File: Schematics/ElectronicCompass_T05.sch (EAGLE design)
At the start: 60 parts, among them Q1 SPB80P06P, Q2 SPB80P06P, Q3 SPB80P06P, Q4 SPB80P06P, U1 ATMEGA32U4, X1 USBSMD

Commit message: board layout continued
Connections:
- net GND: no longer U$1.GND, U$1.NTC
- net N$16: now also U$1.BAT; no longer U$1.GATE
- net N$4: no longer U$1.CLPROG
- net N$5: now also U$1.GATE; no longer U$1.BAT
- net VCC: no longer U$1.ILIM0, U$1.ILIM1
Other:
- moved on the sheet: R4
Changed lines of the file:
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@@
 <part name="GND14" library="supply1" deviceset="GND" device=""/>
 <part name="C2" library="rcl" deviceset="C-US" device="C0805" value="10nF"/>
-<part name="U$1" library="LTC4067" deviceset="LTC4067" device=""/>
 <part name="C3" library="rcl" deviceset="C-US" device="C0805" value="0.1uF"/>
 <part name="TP26" library="testpad" deviceset="TP" device="TP06R"/>
 <part name="TP27" library="testpad" deviceset="TP" device="TP06R"/>
 <part name="TP28" library="testpad" deviceset="TP" device="TP06R"/>
+<part name="U$1" library="LTC4067" deviceset="LTC4067" device=""/>
 </parts>
 <sheets>
@@
 <frame x1="-25.4" y1="-121.92" x2="276.86" y2="88.9" columns="8" rows="5" layer="97"/>
 <text x="243.84" y="-40.64" size="1.778" layer="97">LCD Mounting/TP</text>
-<text x="53.34" y="27.94" size="1.778" layer="97">LTC4067</text>
+<text x="50.8" y="27.94" size="1.778" layer="97">LTC4067</text>
 <text x="210.82" y="10.16" size="1.778" layer="97">LSM303DLM</text>
 <text x="213.36" y="-66.04" size="1.778" layer="97">Nokia 5110</text>
@@
 <instance part="JP6" gate="G$1" x="175.26" y="-86.36"/>
 <instance part="JP7" gate="G$1" x="182.88" y="-86.36"/>
-<instance part="R4" gate="G$1" x="30.48" y="17.78" rot="R90"/>
+<instance part="R4" gate="G$1" x="30.48" y="15.24" rot="R90"/>
 <instance part="R5" gate="G$1" x="27.94" y="55.88"/>
 <instance part="R6" gate="G$1" x="71.12" y="17.78" rot="R270"/>
@@
 <instance part="GND9" gate="1" x="50.8" y="10.16"/>
 <instance part="GND15" gate="1" x="71.12" y="10.16"/>
-<instance part="GND16" gate="1" x="30.48" y="10.16"/>
-<instance part="P+5" gate="VCC" x="25.4" y="38.1"/>
+<instance part="GND16" gate="1" x="30.48" y="7.62"/>
+<instance part="P+5" gate="VCC" x="25.4" y="35.56"/>
 <instance part="LED1" gate="G$1" x="20.32" y="50.8" rot="R180"/>
 <instance part="Q1" gate="G$1" x="12.7" y="48.26" rot="MR270"/>
@@
 <instance part="C12" gate="G$1" x="76.2" y="-17.78"/>
 <instance part="GND17" gate="1" x="76.2" y="-25.4"/>
-<instance part="GND18" gate="1" x="33.02" y="35.56"/>
+<instance part="GND18" gate="1" x="33.02" y="33.02"/>
 <instance part="G1" gate="G$1" x="81.28" y="30.48" rot="R90"/>
 <instance part="GND19" gate="1" x="81.28" y="22.86"/>
@@
 <instance part="GND14" gate="1" x="5.08" y="35.56"/>
 <instance part="C2" gate="G$1" x="10.16" y="68.58"/>
-<instance part="U$1" gate="G$1" x="50.8" y="40.64" rot="R270"/>
 <instance part="C3" gate="G$1" x="121.92" y="7.62"/>
 <instance part="TP26" gate="G$1" x="180.34" y="-33.02" rot="R270"/>
 <instance part="TP27" gate="G$1" x="180.34" y="-48.26" rot="R270"/>
 <instance part="TP28" gate="G$1" x="180.34" y="-43.18" rot="R270"/>
+<instance part="U$1" gate="G$1" x="50.8" y="45.72" rot="R270"/>
 </instances>
 <busses>
@@
 <pinref part="GND18" gate="1" pin="GND"/>
 <pinref part="C5" gate="G$1" pin="2"/>
-<wire x1="30.48" y1="38.1" x2="33.02" y2="38.1" width="0.1524" layer="91"/>
-<pinref part="U$1" gate="G$1" pin="NTC"/>
-<junction x="33.02" y="38.1"/>
+<wire x1="30.48" y1="38.1" x2="30.48" y2="35.56" width="0.1524" layer="91"/>
+<wire x1="30.48" y1="35.56" x2="33.02" y2="35.56" width="0.1524" layer="91"/>
 </segment>
 <segment>
 <pinref part="C11" gate="G$1" pin="2"/>
 <pinref part="GND14" gate="1" pin="GND"/>
-</segment>
-<segment>
-<pinref part="GND9" gate="1" pin="GND"/>
-<pinref part="U$1" gate="G$1" pin="GND"/>
 </segment>
 <segment>
@@
 </segment>
 <segment>
-<wire x1="33.02" y1="27.94" x2="25.4" y2="27.94" width="0.1524" layer="91"/>
+<wire x1="33.02" y1="25.4" x2="25.4" y2="25.4" width="0.1524" layer="91"/>
 <pinref part="P+5" gate="VCC" pin="VCC"/>
-<wire x1="25.4" y1="27.94" x2="25.4" y2="33.02" width="0.1524" layer="91"/>
-<wire x1="25.4" y1="33.02" x2="25.4" y2="35.56" width="0.1524" layer="91"/>
-<wire x1="33.02" y1="33.02" x2="25.4" y2="33.02" width="0.1524" layer="91"/>
-<junction x="25.4" y="33.02"/>
-<pinref part="U$1" gate="G$1" pin="ILIM0"/>
-<pinref part="U$1" gate="G$1" pin="ILIM1"/>
+<wire x1="25.4" y1="25.4" x2="25.4" y2="30.48" width="0.1524" layer="91"/>
+<wire x1="25.4" y1="30.48" x2="25.4" y2="33.02" width="0.1524" layer="91"/>
+<wire x1="33.02" y1="30.48" x2="25.4" y2="30.48" width="0.1524" layer="91"/>
+<junction x="25.4" y="30.48"/>
 </segment>
 </net>
@@
 <segment>
 <pinref part="R4" gate="G$1" pin="2"/>
-<wire x1="30.48" y1="22.86" x2="33.02" y2="22.86" width="0.1524" layer="91"/>
-<pinref part="U$1" gate="G$1" pin="CLPROG"/>
+<wire x1="30.48" y1="20.32" x2="33.02" y2="20.32" width="0.1524" layer="91"/>
 </segment>
 </net>
@@
 <wire x1="81.28" y1="38.1" x2="81.28" y2="45.72" width="0.1524" layer="91"/>
 <junction x="81.28" y="38.1"/>
-<pinref part="U$1" gate="G$1" pin="BAT"/>
+<pinref part="U$1" gate="G$1" pin="GATE"/>
 </segment>
 </net>
@@
 <pinref part="Q2" gate="G$1" pin="G"/>
 <wire x1="68.58" y1="53.34" x2="76.2" y2="53.34" width="0.1524" layer="91"/>
-<pinref part="U$1" gate="G$1" pin="GATE"/>
+<pinref part="U$1" gate="G$1" pin="BAT"/>
 </segment>
 </net>
@@
 </segment>
 </net>
-<net name="N$7" class="0">
-<segment>
-<pinref part="R5" gate="G$1" pin="2"/>
-<pinref part="U$1" gate="G$1" pin="CHARGE"/>
-</segment>
-</net>
 <net name="N$37" class="0">
 <segment>
@@
 </segment>
 </net>
+<net name="N$7" class="0">
+<segment>
+<pinref part="R5" gate="G$1" pin="2"/>
+<pinref part="U$1" gate="G$1" pin="CHARGE"/>
+</segment>
+</net>

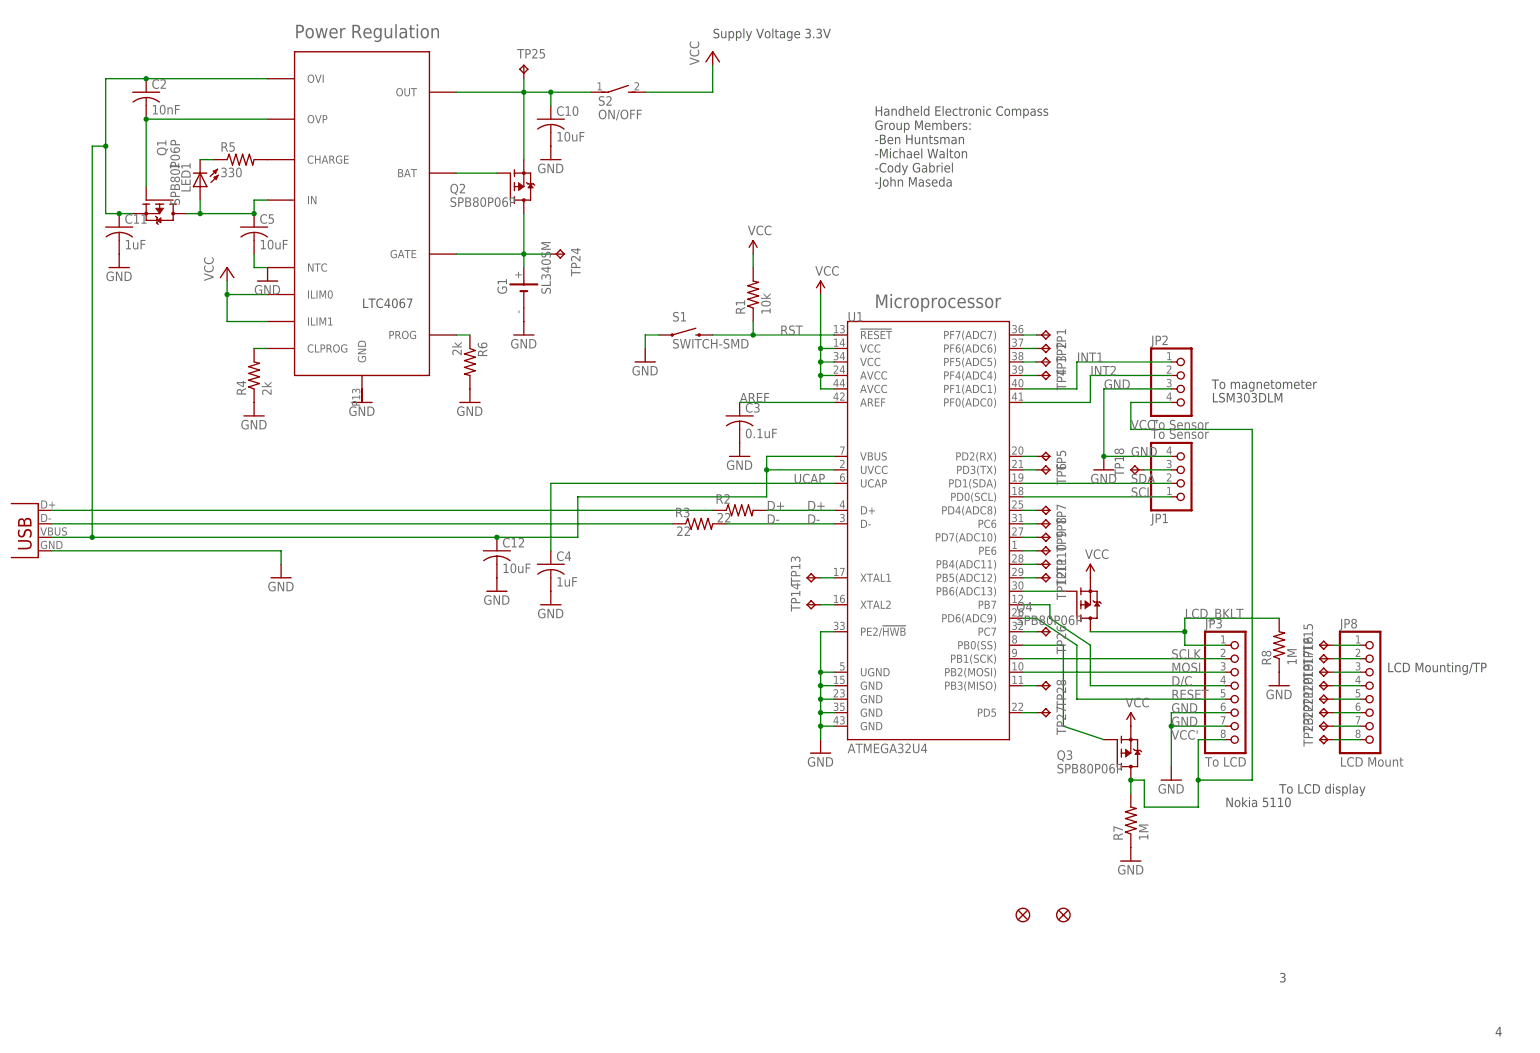
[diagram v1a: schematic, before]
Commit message: New transistors
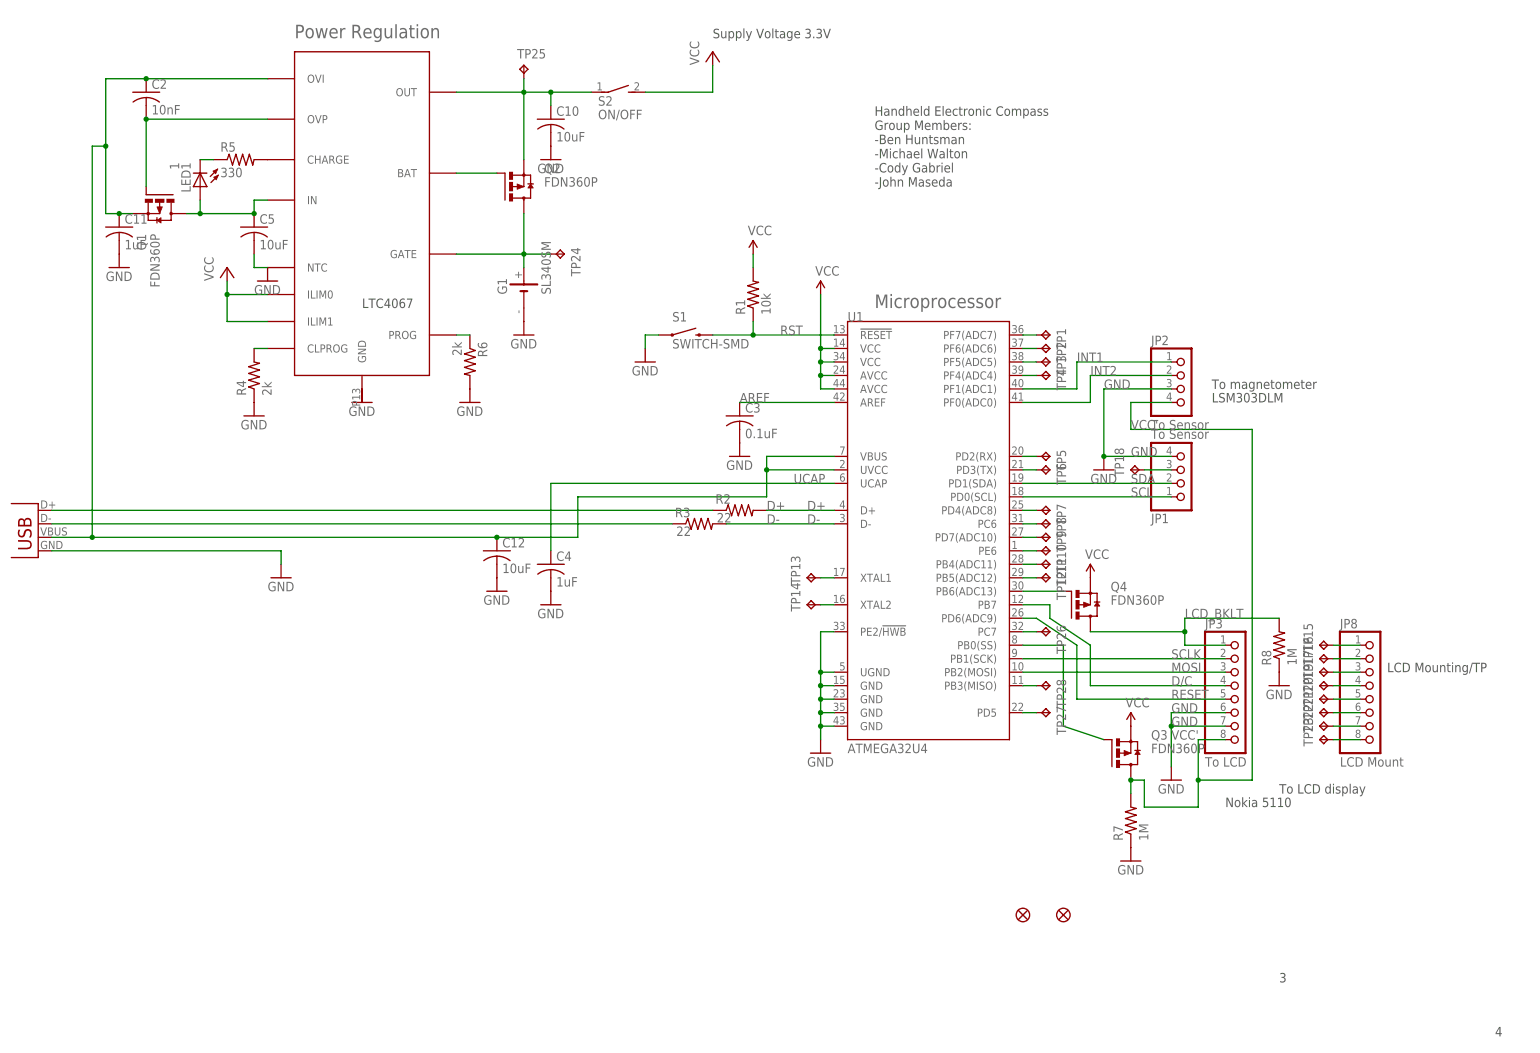
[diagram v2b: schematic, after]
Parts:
- Q1, Q2, Q3, Q4: value SPB80P06P -> FDN360P; device transistor-fet:SPB80P06P -> transistor-power:FDN360P
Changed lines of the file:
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@@
 <part name="P+5" library="supply1" deviceset="VCC" device=""/>
 <part name="LED1" library="led" deviceset="LED" device="CHIPLED_0805" value="1"/>
-<part name="Q1" library="transistor-fet" deviceset="SPB80P06P" device=""/>
-<part name="Q2" library="transistor-fet" deviceset="SPB80P06P" device=""/>
+<part name="Q2" library="transistor-power" deviceset="FDN360P" device=""/>
 <part name="C12" library="rcl" deviceset="C-US" device="C0805" value="10uF"/>
 <part name="GND17" library="supply1" deviceset="GND" device=""/>
@@
 <part name="GND8" library="supply1" deviceset="GND" device=""/>
 <part name="GND10" library="supply1" deviceset="GND" device=""/>
-<part name="Q3" library="transistor-fet" deviceset="SPB80P06P" device=""/>
-<part name="Q4" library="transistor-fet" deviceset="SPB80P06P" device=""/>
+<part name="Q3" library="transistor-power" deviceset="FDN360P" device=""/>
 <part name="R7" library="rcl" deviceset="R-US_" device="M0805" value="1M"/>
 <part name="R8" library="rcl" deviceset="R-US_" device="M0805" value="1M"/>
@@
 <part name="TP28" library="testpad" deviceset="TP" device="TP06R"/>
 <part name="U$1" library="LTC4067" deviceset="LTC4067" device=""/>
+<part name="Q4" library="transistor-power" deviceset="FDN360P" device=""/>
+<part name="Q1" library="transistor-power" deviceset="FDN360P" device=""/>
 </parts>
 <sheets>
@@
 <instance part="P+5" gate="VCC" x="25.4" y="35.56"/>
 <instance part="LED1" gate="G$1" x="20.32" y="50.8" rot="R180"/>
-<instance part="Q1" gate="G$1" x="12.7" y="48.26" rot="MR270"/>
 <instance part="Q2" gate="G$1" x="78.74" y="50.8"/>
 <instance part="C12" gate="G$1" x="76.2" y="-17.78"/>
@@
 <instance part="GND10" gate="1" x="203.2" y="-60.96"/>
 <instance part="Q3" gate="G$1" x="193.04" y="-55.88"/>
-<instance part="Q4" gate="G$1" x="185.42" y="-27.94"/>
 <instance part="R7" gate="G$1" x="195.58" y="-68.58" rot="R90"/>
 <instance part="R8" gate="G$1" x="223.52" y="-35.56" rot="R90"/>
@@
 <instance part="TP28" gate="G$1" x="180.34" y="-43.18" rot="R270"/>
 <instance part="U$1" gate="G$1" x="50.8" y="45.72" rot="R270"/>
+<instance part="Q4" gate="G$1" x="185.42" y="-27.94"/>
+<instance part="Q1" gate="G$1" x="12.7" y="48.26" rot="MR270"/>
 </instances>
 <busses>
@@
 </segment>
 <segment>
-<pinref part="Q4" gate="G$1" pin="S"/>
-<pinref part="P+4" gate="1" pin="VCC"/>
-</segment>
-<segment>
 <pinref part="Q3" gate="G$1" pin="S"/>
 <pinref part="P+6" gate="1" pin="VCC"/>
@@
 <wire x1="33.02" y1="30.48" x2="25.4" y2="30.48" width="0.1524" layer="91"/>
 <junction x="25.4" y="30.48"/>
+</segment>
+<segment>
+<pinref part="P+4" gate="1" pin="VCC"/>
+<pinref part="Q4" gate="G$1" pin="S"/>
 </segment>
 </net>
@@
 <segment>
 <pinref part="U1" gate="G$1" pin="PB6(ADC13)"/>
+<wire x1="175.26" y1="-25.4" x2="182.88" y2="-25.4" width="0.1524" layer="91"/>
 <pinref part="Q4" gate="G$1" pin="G"/>
-<wire x1="175.26" y1="-25.4" x2="182.88" y2="-25.4" width="0.1524" layer="91"/>
 </segment>
 </net>
@@
 <wire x1="205.74" y1="-33.02" x2="205.74" y2="-35.56" width="0.1524" layer="91"/>
 <wire x1="205.74" y1="-35.56" x2="213.36" y2="-35.56" width="0.1524" layer="91"/>
-<pinref part="Q4" gate="G$1" pin="D"/>
 <wire x1="187.96" y1="-33.02" x2="205.74" y2="-33.02" width="0.1524" layer="91"/>
 <junction x="205.74" y="-33.02"/>
+<pinref part="Q4" gate="G$1" pin="D"/>
 </segment>
 </net>
@@
 <net name="N$6" class="0">
 <segment>
-<pinref part="Q1" gate="G$1" pin="D"/>
 <wire x1="17.78" y1="45.72" x2="20.32" y2="45.72" width="0.1524" layer="91"/>
 <wire x1="20.32" y1="45.72" x2="30.48" y2="45.72" width="0.1524" layer="91"/>
@@
 <junction x="20.32" y="45.72"/>
 <pinref part="U$1" gate="G$1" pin="IN"/>
+<pinref part="Q1" gate="G$1" pin="D"/>
 </segment>
 </net>
@@
 <net name="N$9" class="0">
 <segment>
-<pinref part="Q1" gate="G$1" pin="G"/>
 <wire x1="10.16" y1="50.8" x2="10.16" y2="63.5" width="0.1524" layer="91"/>
 <wire x1="10.16" y1="63.5" x2="33.02" y2="63.5" width="0.1524" layer="91"/>
@@
 <junction x="10.16" y="63.5"/>
 <pinref part="U$1" gate="G$1" pin="OVP"/>
+<pinref part="Q1" gate="G$1" pin="G"/>
 </segment>
 </net>
@@
 <wire x1="10.16" y1="71.12" x2="2.54" y2="71.12" width="0.1524" layer="91"/>
 <wire x1="2.54" y1="71.12" x2="2.54" y2="58.42" width="0.1524" layer="91"/>
-<pinref part="Q1" gate="G$1" pin="S"/>
 <wire x1="2.54" y1="58.42" x2="2.54" y2="45.72" width="0.1524" layer="91"/>
 <wire x1="2.54" y1="45.72" x2="5.08" y2="45.72" width="0.1524" layer="91"/>
@@
 <junction x="2.54" y="58.42"/>
 <pinref part="U$1" gate="G$1" pin="OVI"/>
-</segment>
-</net>
+<pinref part="Q1" gate="G$1" pin="S"/>
+</segment>
+</net>

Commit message: xtal added
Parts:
- removed TP13, TP14: TPTP06R, testpad:TPTP06R
- added C1, C6: 18pF, SparkFun:CAP0402-CAP
- added Y1: 16MHz, SparkFun:CRYSTAL5X3
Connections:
- new net N$41: C1.2, Y1.2
- new net N$42: C6.2, Y1.1
- net GND: now also C1.1, C6.1
- net N$2: no longer TP13.TP
- net N$3: no longer TP14.TP
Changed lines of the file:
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@@
 <part name="P+4" library="SparkFun" deviceset="VCC" device=""/>
 <part name="P+6" library="SparkFun" deviceset="VCC" device=""/>
-<part name="TP13" library="testpad" deviceset="TP" device="TP06R"/>
-<part name="TP14" library="testpad" deviceset="TP" device="TP06R"/>
 <part name="JP8" library="pinhead" deviceset="PINHD-1X8" device="" value="LCD Mount"/>
 <part name="TP15" library="testpad" deviceset="TP" device="TP06R"/>
@@
 <part name="Q4" library="transistor-power" deviceset="FDN360P" device=""/>
 <part name="Q1" library="transistor-power" deviceset="FDN360P" device=""/>
+<part name="Y1" library="SparkFun" deviceset="CRYSTAL" device="5X3" value="16MHz"/>
+<part name="C1" library="SparkFun" deviceset="CAP" device="0402-CAP" value="18pF"/>
+<part name="C6" library="SparkFun" deviceset="CAP" device="0402-CAP" value="18pF"/>
+<part name="GND3" library="SparkFun" deviceset="GND" device=""/>
 </parts>
 <sheets>
@@
 <instance part="P+4" gate="1" x="187.96" y="-22.86"/>
 <instance part="P+6" gate="1" x="195.58" y="-50.8"/>
-<instance part="TP13" gate="G$1" x="134.62" y="-22.86" rot="R90"/>
-<instance part="TP14" gate="G$1" x="134.62" y="-27.94" rot="R90"/>
 <instance part="JP8" gate="A" x="241.3" y="-45.72"/>
 <instance part="TP15" gate="G$1" x="231.14" y="-35.56" rot="R90"/>
@@
 <instance part="Q4" gate="G$1" x="185.42" y="-27.94"/>
 <instance part="Q1" gate="G$1" x="12.7" y="48.26" rot="MR270"/>
+<instance part="Y1" gate="G$1" x="132.08" y="-25.4" smashed="yes" rot="R90">
+<attribute name="NAME" x="133.35" y="-20.32" size="1.778" layer="95" rot="R180"/>
+<attribute name="VALUE" x="135.636" y="-28.956" size="1.778" layer="96" rot="R180"/>
+</instance>
+<instance part="C1" gate="G$1" x="124.46" y="-22.86" smashed="yes" rot="R90">
+<attribute name="NAME" x="121.92" y="-20.193" size="1.778" layer="95" rot="R180"/>
+<attribute name="VALUE" x="129.54" y="-19.939" size="1.778" layer="96" rot="R180"/>
+</instance>
+<instance part="C6" gate="G$1" x="124.46" y="-27.94" smashed="yes" rot="R90">
+<attribute name="NAME" x="121.92" y="-25.527" size="1.778" layer="95" rot="R180"/>
+<attribute name="VALUE" x="129.54" y="-25.273" size="1.778" layer="96" rot="R180"/>
+</instance>
+<instance part="GND3" gate="1" x="114.3" y="-30.48"/>
 </instances>
 <busses>
@@
 <pinref part="C3" gate="G$1" pin="2"/>
 </segment>
+<segment>
+<wire x1="119.38" y1="-27.94" x2="116.84" y2="-27.94" width="0.1524" layer="91"/>
+<wire x1="116.84" y1="-27.94" x2="116.84" y2="-25.4" width="0.1524" layer="91"/>
+<wire x1="116.84" y1="-25.4" x2="116.84" y2="-22.86" width="0.1524" layer="91"/>
+<wire x1="116.84" y1="-22.86" x2="119.38" y2="-22.86" width="0.1524" layer="91"/>
+<wire x1="116.84" y1="-25.4" x2="114.3" y2="-25.4" width="0.1524" layer="91"/>
+<wire x1="114.3" y1="-25.4" x2="114.3" y2="-27.94" width="0.1524" layer="91"/>
+<junction x="116.84" y="-25.4"/>
+<pinref part="C6" gate="G$1" pin="1"/>
+<pinref part="C1" gate="G$1" pin="1"/>
+<pinref part="GND3" gate="1" pin="GND"/>
+</segment>
 </net>
 <net name="VCC" class="0">
@@
 <net name="N$2" class="0">
 <segment>
-<pinref part="TP13" gate="G$1" pin="TP"/>
 <pinref part="U1" gate="G$1" pin="XTAL1"/>
 <wire x1="137.16" y1="-22.86" x2="139.7" y2="-22.86" width="0.1524" layer="91"/>
@@
 <net name="N$3" class="0">
 <segment>
-<pinref part="TP14" gate="G$1" pin="TP"/>
 <pinref part="U1" gate="G$1" pin="XTAL2"/>
 <wire x1="137.16" y1="-27.94" x2="139.7" y2="-27.94" width="0.1524" layer="91"/>
@@
 </segment>
 </net>
+<net name="N$41" class="0">
+<segment>
+<wire x1="127" y1="-22.86" x2="132.08" y2="-22.86" width="0.1524" layer="91"/>
+<wire x1="132.08" y1="-22.86" x2="137.16" y2="-22.86" width="0.1524" layer="91"/>
+<junction x="132.08" y="-22.86"/>
+<pinref part="C1" gate="G$1" pin="2"/>
+<pinref part="Y1" gate="G$1" pin="2"/>
+</segment>
+</net>
+<net name="N$42" class="0">
+<segment>
+<wire x1="137.16" y1="-27.94" x2="132.08" y2="-27.94" width="0.1524" layer="91"/>
+<wire x1="132.08" y1="-27.94" x2="127" y2="-27.94" width="0.1524" layer="91"/>
+<junction x="132.08" y="-27.94"/>
+<pinref part="Y1" gate="G$1" pin="1"/>
+<pinref part="C6" gate="G$1" pin="2"/>
+</segment>
+</net>

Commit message: gpio change push
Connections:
- removed net N$2 (its old number): U1.XTAL1
- removed net N$26 (its old number): TP12.TP, U1.PB5(ADC12)
- net D/C: now also U1.PB4(ADC11); no longer U1.PB7
- net GND: now also U$1.GND, U$1.NTC
- net N$25: now also U1.PB7; no longer U1.PB4(ADC11)
- net N$3: now also TP12.TP, U1.PD6(ADC9); no longer U1.XTAL2
- net N$4: now also U$1.CLPROG
- net N$41: now also U1.XTAL1
- net N$42: now also U1.XTAL2
- net RESET: now also U1.PB5(ADC12); no longer U1.PD6(ADC9)
- net VCC: now also U$1.ILIM0, U$1.ILIM1
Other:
- moved on the sheet: C1, C6, Q4, TP11, TP12, Y1
